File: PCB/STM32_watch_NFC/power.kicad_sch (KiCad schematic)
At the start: 6 parts, among them J2 USB_C_Receptacle_PowerOnly_6P, U2 MIC5365-3.3YC5

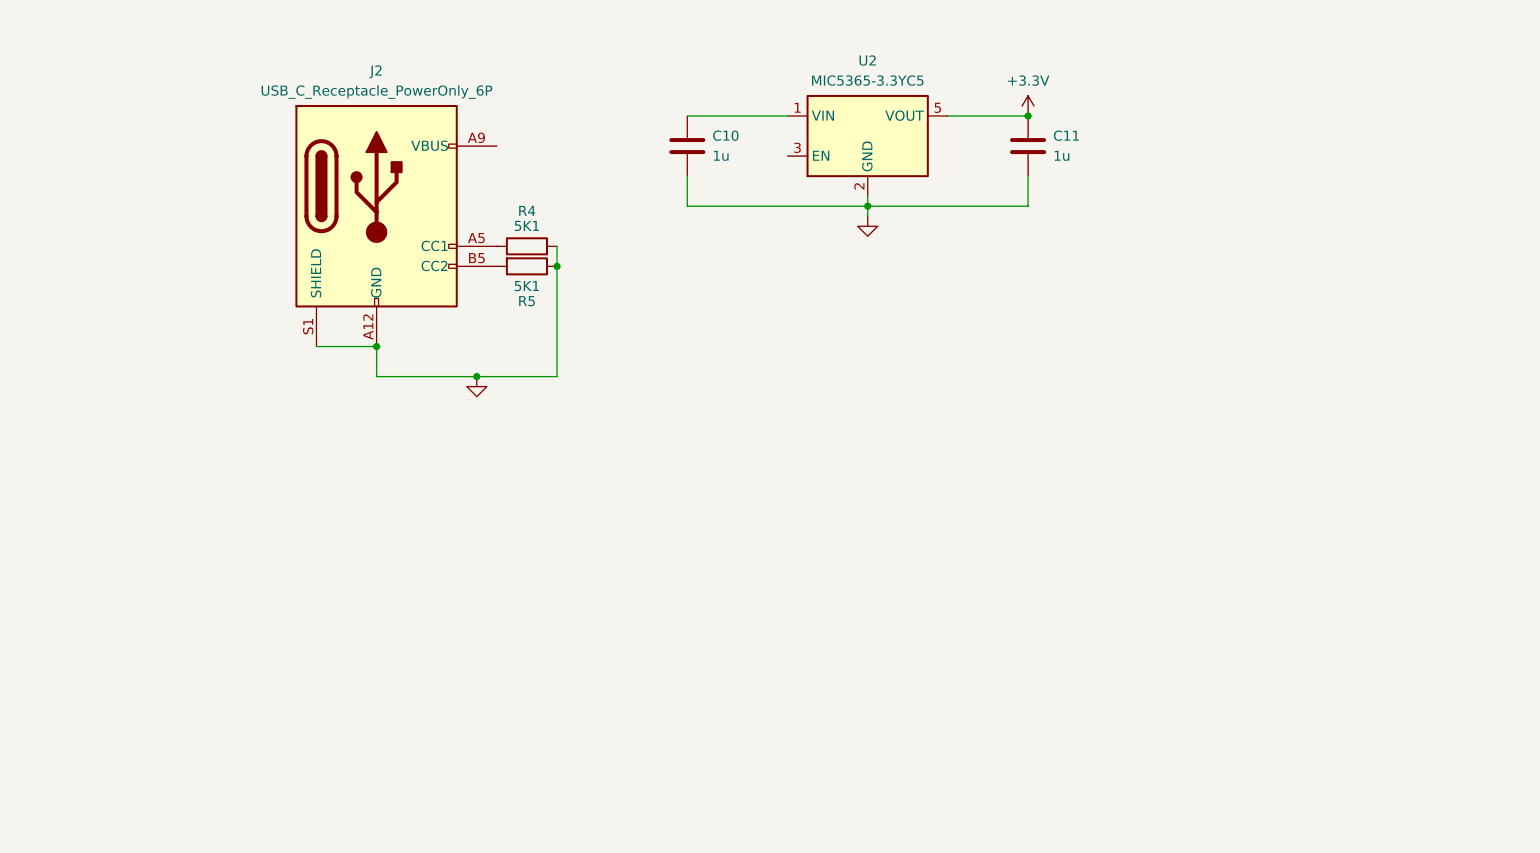
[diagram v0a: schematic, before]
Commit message: Kicad
Everything about power, started to make nfc - spiral antenna problem
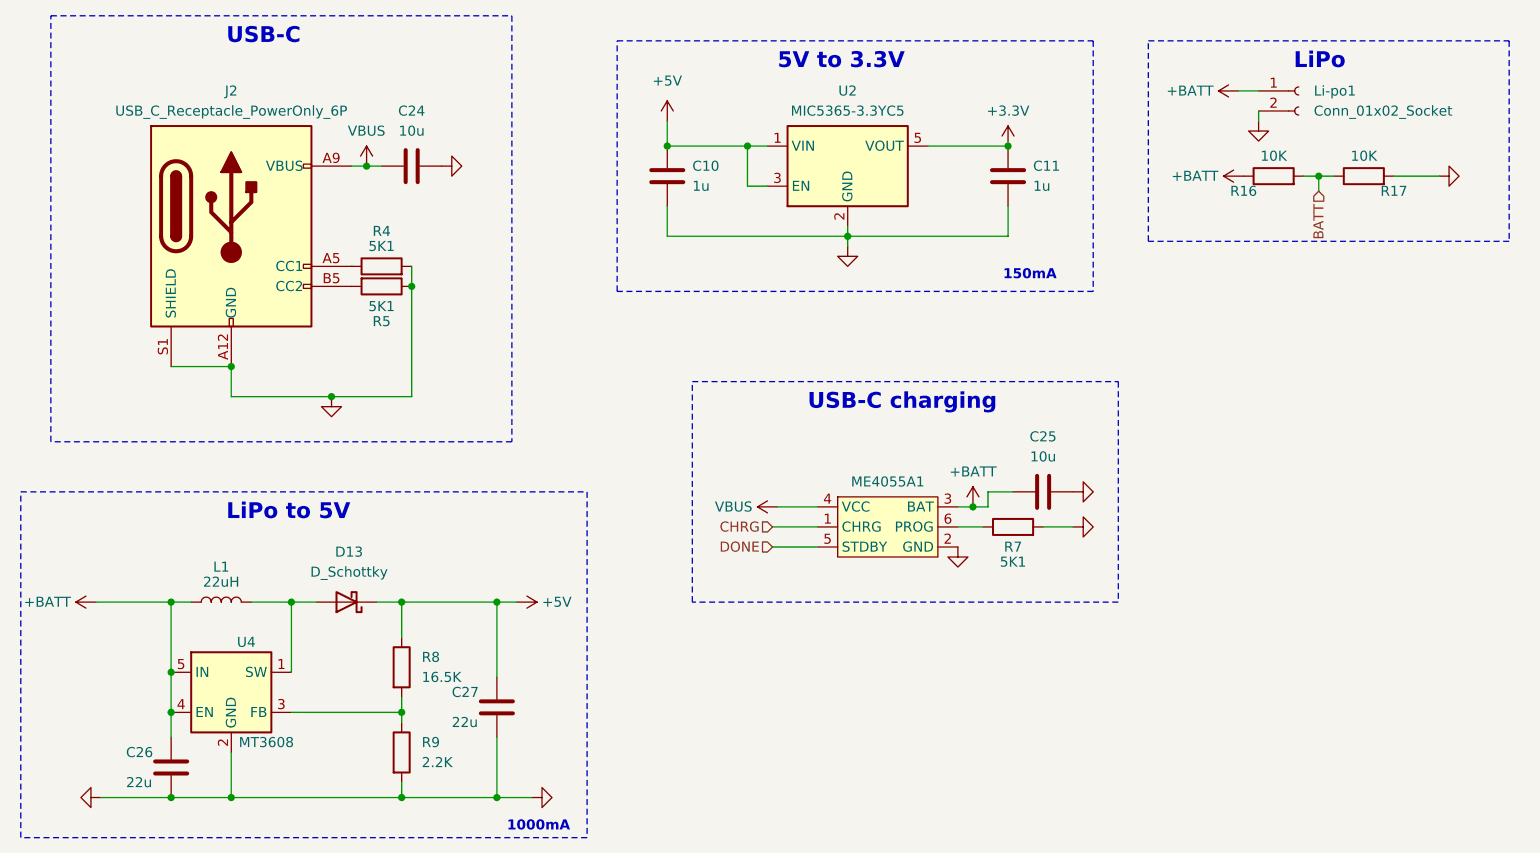
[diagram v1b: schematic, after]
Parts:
- added C24, C25: 10u, Capacitor_SMD:C_0603_1608Metric, symbol Device:C
- added C26, C27: 22u, Capacitor_SMD:C_0603_1608Metric, symbol Device:C
- added D13: D_Schottky, symbol Device:D_Schottky
- added L1: 22uH, symbol Device:L
- added Li-po1: Conn_01x02_Socket, Connector_JST:JST_SUR_SM02B-SURS-TF_1x02-1MP_P0.80mm_Horizontal, symbol Connector:Conn_01x02_Socket
- added ME4055A1: ~, Package_TO_SOT_SMD:SOT-23-6, symbol Power:ME4055AM6G
- added R16, R17: 10K, Resistor_SMD:R_0402_1005Metric, symbol Device:R
- added R7: 5K1, Resistor_SMD:R_0402_1005Metric, symbol Device:R
- added R8: 16.5K, symbol Device:R
- added R9: 2.2K, symbol Device:R
- added U4: MT3608, Package_TO_SOT_SMD:SOT-23-6, symbol Regulator_Switching:MT3608
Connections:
- net GND: now also C24.2, C25.2, C26.2, C27.2, Li-po1.2 (Pin_2), ME4055A1.2 (GND), R17.2, R7.2, R9.2, U4.2 (GND)
- net +5V: now reaches C10.2, U2.1 (VIN)
- net +5V: now also U2.3 (EN), C27.1, D13.1 (K), R8.1
- net VBUS: now reaches J2.A9 (VBUS), J2.B9 (VBUS)
- net VBUS: now also C24.1, ME4055A1.4 (VCC)
- new net: ME4055A1.6 (PROG), R7.1
- new net: R8.2, R9.1, U4.3 (FB)
- new net: D13.2 (A), L1.2, U4.1 (SW)
- new net +BATT: C25.1, C26.1, L1.1, Li-po1.1 (Pin_1), ME4055A1.3 (BAT), R16.1, U4.4 (EN), U4.5 (IN)
- new net BATT: R16.2, R17.1
- new net CHRG: ME4055A1.1 (CHRG)
- new net DONE: ME4055A1.5 (STDBY)
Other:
- note added: "1000mA"
- note added: "150mA"
- note added: "5V to 3.3V"
- note added: "LiPo"
- note added: "LiPo to 5V"
- note added: "USB-C"
- note added: "USB-C charging"
- moved on the sheet: C10, C11, J2, R4, R5, U2

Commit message: Kicad - LCSC, footprints
I managed to add all (I hope so :) ) LCSC values - which component will be used. With that I could determine all footprints
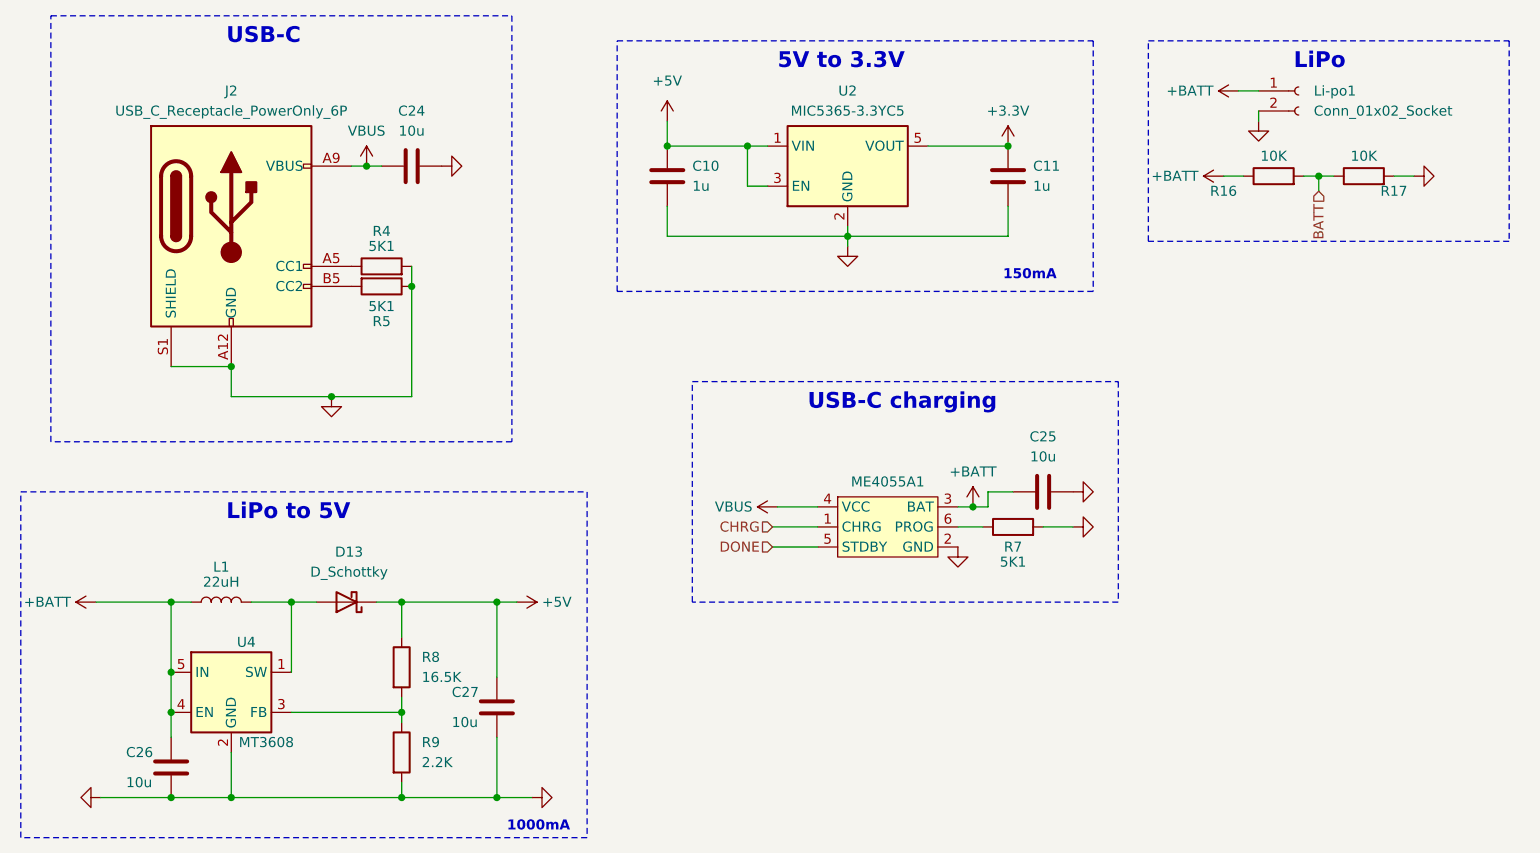
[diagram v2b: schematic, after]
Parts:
- C10, C11: LCSC (none) -> C412453
- C24, C25: LCSC (none) -> C77040
- C26, C27: value 22u -> 10u; LCSC (none) -> C77040
- D13: footprint (none) -> Diode_SMD:D_SOD-523; LCSC (none) -> C145179
- J2: footprint Connector_USB:USB_C_Receptacle_GCT_USB4125-xx-x-0190_6P_TopMnt_Horizontal -> Connector_USB:USB_C_Receptacle_GCT_USB4135-GF-A_6P_TopMnt_Horizontal; LCSC (none) -> C2927283
- L1: footprint (none) -> Components:SLW3015; LCSC (none) -> C206322
- ME4055A1: LCSC (none) -> C610261
- R16, R17: LCSC (none) -> C308028
- R4, R5, R7: LCSC (none) -> C284599
- R8: footprint (none) -> Resistor_SMD:R_0805_2012Metric; LCSC (none) -> C104028
- R9: footprint (none) -> Resistor_SMD:R_0402_1005Metric; LCSC (none) -> C509322
- U2: LCSC (none) -> C3021118
- U4: LCSC (none) -> C84817
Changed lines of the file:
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@@
+    (stroke (width 0) (type default))
+  )
+  (wire (pts (xy 175.895 41.275) (xy 178.435 41.275))
     (stroke (width 0) (type default))
   )
@@
     (stroke (width 0) (type default))
   )
-  (wire (pts (xy 197.485 41.275) (xy 203.2 41.275))
+  (wire (pts (xy 197.485 41.275) (xy 200.025 41.275))
     (stroke (width 0) (type default))
   )
@@
       (effects (font (size 1.27 1.27)) hide)
     )
+    (property "LCSC" "C284599" (at 149.225 85.725 90)
+      (effects (font (size 1.27 1.27)) hide)
+    )
     (pin "1")
     (pin "2")
@@
       (effects (font (size 1.27 1.27)) (justify left))
     )
-    (property "Footprint" "" (at 69.977 114.3 90)
+    (property "Footprint" "Resistor_SMD:R_0402_1005Metric" (at 69.977 114.3 90)
       (effects (font (size 1.27 1.27)) hide)
     )
     (property "Datasheet" "~" (at 71.755 114.3 0)
+      (effects (font (size 1.27 1.27)) hide)
+    )
+    (property "LCSC" "C509322" (at 71.755 114.3 0)
       (effects (font (size 1.27 1.27)) hide)
     )
@@
     )
     (property "Datasheet" "~" (at 105.41 41.275 0)
+      (effects (font (size 1.27 1.27)) hide)
+    )
+    (property "LCSC" "C412453" (at 105.41 41.275 0)
       (effects (font (size 1.27 1.27)) hide)
     )
@@
       (effects (font (size 1.27 1.27)) (justify left))
     )
-    (property "Value" "22u" (at 36.83 118.11 0)
+    (property "Value" "10u" (at 36.83 118.11 0)
       (effects (font (size 1.27 1.27)) (justify left))
     )
@@
     )
     (property "Datasheet" "~" (at 42.545 116.205 0)
+      (effects (font (size 1.27 1.27)) hide)
+    )
+    (property "LCSC" "C77040" (at 42.545 116.205 0)
       (effects (font (size 1.27 1.27)) hide)
     )
@@
       (effects (font (size 1.27 1.27)) (justify left))
     )
-    (property "Value" "22u" (at 78.105 110.49 0)
+    (property "Value" "10u" (at 78.105 110.49 0)
       (effects (font (size 1.27 1.27)) (justify left))
     )
@@
     )
     (property "Datasheet" "~" (at 83.82 108.585 0)
+      (effects (font (size 1.27 1.27)) hide)
+    )
+    (property "LCSC" "C77040" (at 83.82 108.585 0)
       (effects (font (size 1.27 1.27)) hide)
     )
@@
       (effects (font (size 1.27 1.27)))
     )
-    (property "Footprint" "Connector_USB:USB_C_Receptacle_GCT_USB4125-xx-x-0190_6P_TopMnt_Horizontal" (at 53.975 45.085 0)
+    (property "Footprint" "Connector_USB:USB_C_Receptacle_GCT_USB4135-GF-A_6P_TopMnt_Horizontal" (at 53.975 45.085 0)
       (effects (font (size 1.27 1.27)) hide)
     )
     (property "Datasheet" "https://www.usb.org/sites/default/files/documents/usb_type-c.zip" (at 50.165 47.625 0)
+      (effects (font (size 1.27 1.27)) hide)
+    )
+    (property "LCSC" "C2927283" (at 50.165 47.625 0)
       (effects (font (size 1.27 1.27)) hide)
     )
@@
       (effects (font (size 1.27 1.27)) hide)
     )
+    (property "LCSC" "C284599" (at 69.215 55.245 90)
+      (effects (font (size 1.27 1.27)) hide)
+    )
     (pin "1")
     (pin "2")
@@
     )
   )
-  (symbol (lib_id "power:+BATT") (at 178.435 41.275 90) (unit 1)
-    (in_bom yes) (on_board yes) (dnp no) (fields_autoplaced)
-    (property "Reference" "#PWR075" (at 182.245 41.275 0)
-      (effects (font (size 1.27 1.27)) hide)
-    )
-    (property "Value" "+BATT" (at 175.26 41.275 90)
-      (effects (font (size 1.27 1.27)) (justify left))
-    )
-    (property "Footprint" "" (at 178.435 41.275 0)
-      (effects (font (size 1.27 1.27)) hide)
-    )
-    (property "Datasheet" "" (at 178.435 41.275 0)
+  (symbol (lib_id "power:+BATT") (at 175.895 41.275 90) (unit 1)
+    (in_bom yes) (on_board yes) (dnp no) (fields_autoplaced)
+    (property "Reference" "#PWR075" (at 179.705 41.275 0)
+      (effects (font (size 1.27 1.27)) hide)
+    )
+    (property "Value" "+BATT" (at 172.72 41.275 90)
+      (effects (font (size 1.27 1.27)) (justify left))
+    )
+    (property "Footprint" "" (at 175.895 41.275 0)
+      (effects (font (size 1.27 1.27)) hide)
+    )
+    (property "Datasheet" "" (at 175.895 41.275 0)
       (effects (font (size 1.27 1.27)) hide)
     )
@@
       (effects (font (size 1.27 1.27)))
     )
-    (property "Footprint" "" (at 48.895 95.25 0)
+    (property "Footprint" "Components:SLW3015" (at 48.895 95.25 0)
       (effects (font (size 1.27 1.27)) hide)
     )
@@
       (effects (font (size 1.27 1.27)) hide)
     )
+    (property "LCSC" "C206322" (at 48.895 95.25 90)
+      (effects (font (size 1.27 1.27)) hide)
+    )
     (pin "2")
     (pin "1")
@@
     )
   )
-  (symbol (lib_id "power:GND") (at 203.2 41.275 90) (unit 1)
-    (in_bom yes) (on_board yes) (dnp no) (fields_autoplaced)
-    (property "Reference" "#PWR074" (at 209.55 41.275 0)
-      (effects (font (size 1.27 1.27)) hide)
-    )
-    (property "Value" "GND" (at 208.28 41.275 0)
-      (effects (font (size 1.27 1.27)) hide)
-    )
-    (property "Footprint" "" (at 203.2 41.275 0)
-      (effects (font (size 1.27 1.27)) hide)
-    )
-    (property "Datasheet" "" (at 203.2 41.275 0)
+  (symbol (lib_id "power:GND") (at 200.025 41.275 90) (unit 1)
+    (in_bom yes) (on_board yes) (dnp no) (fields_autoplaced)
+    (property "Reference" "#PWR074" (at 206.375 41.275 0)
+      (effects (font (size 1.27 1.27)) hide)
+    )
+    (property "Value" "GND" (at 205.105 41.275 0)
+      (effects (font (size 1.27 1.27)) hide)
+    )
+    (property "Footprint" "" (at 200.025 41.275 0)
+      (effects (font (size 1.27 1.27)) hide)
+    )
+    (property "Datasheet" "" (at 200.025 41.275 0)
       (effects (font (size 1.27 1.27)) hide)
     )
@@
       (effects (font (size 1.27 1.27)) hide)
     )
+    (property "LCSC" "C77040" (at 153.035 81.28 90)
+      (effects (font (size 1.27 1.27)) hide)
+    )
     (pin "2")
     (pin "1")
@@
     )
     (property "Datasheet" "" (at 130.81 84.455 0)
+      (effects (font (size 1.27 1.27)) hide)
+    )
+    (property "LCSC" "C610261" (at 133.35 84.455 0)
       (effects (font (size 1.27 1.27)) hide)
     )
@@
       (effects (font (size 1.27 1.27)))
     )
-    (property "Footprint" "" (at 64.77 95.25 0)
+    (property "Footprint" "Diode_SMD:D_SOD-523" (at 64.77 95.25 0)
       (effects (font (size 1.27 1.27)) hide)
     )
     (property "Datasheet" "~" (at 64.77 95.25 0)
+      (effects (font (size 1.27 1.27)) hide)
+    )
+    (property "LCSC" "C145179" (at 64.77 95.25 0)
       (effects (font (size 1.27 1.27)) hide)
     )
@@
   (symbol (lib_id "Device:R") (at 182.245 41.275 90) (unit 1)
     (in_bom yes) (on_board yes) (dnp no)
-    (property "Reference" "R16" (at 178.435 43.18 90)
+    (property "Reference" "R16" (at 175.895 43.18 90)
       (effects (font (size 1.27 1.27)))
     )
@@
     )
     (property "Datasheet" "~" (at 182.245 41.275 0)
+      (effects (font (size 1.27 1.27)) hide)
+    )
+    (property "LCSC" "C308028" (at 182.245 41.275 90)
       (effects (font (size 1.27 1.27)) hide)
     )
@@
       (effects (font (size 1.27 1.27)) hide)
     )
+    (property "LCSC" "C308028" (at 193.675 41.275 90)
+      (effects (font (size 1.27 1.27)) hide)
+    )
     (pin "1")
     (pin "2")
@@
       (effects (font (size 1.27 1.27)) (justify left))
     )
-    (property "Footprint" "" (at 69.977 103.505 90)
+    (property "Footprint" "Resistor_SMD:R_0805_2012Metric" (at 69.977 103.505 90)
       (effects (font (size 1.27 1.27)) hide)
     )
@@
       (effects (font (size 1.27 1.27)) hide)
     )
+    (property "LCSC" "C104028" (at 71.755 103.505 0)
+      (effects (font (size 1.27 1.27)) hide)
+    )
     (pin "2")
     (pin "1")
@@
     )
     (property "Datasheet" "http://ww1.microchip.com/downloads/en/DeviceDoc/mic5365.pdf" (at 120.65 19.685 0)
+      (effects (font (size 1.27 1.27)) hide)
+    )
+    (property "LCSC" "C3021118" (at 128.27 40.005 0)
       (effects (font (size 1.27 1.27)) hide)
     )
@@
     )
     (property "Datasheet" "~" (at 148.59 41.275 0)
+      (effects (font (size 1.27 1.27)) hide)
+    )
+    (property "LCSC" "C412453" (at 148.59 41.275 0)
       (effects (font (size 1.27 1.27)) hide)
     )
@@
       (effects (font (size 1.27 1.27)) hide)
     )
+    (property "LCSC" "C284599" (at 69.215 52.705 90)
+      (effects (font (size 1.27 1.27)) hide)
+    )
     (pin "1")
     (pin "2")
@@
     )
     (property "Datasheet" "~" (at 73.025 40.005 0)
+      (effects (font (size 1.27 1.27)) hide)
+    )
+    (property "LCSC" "C77040" (at 73.025 40.005 90)
       (effects (font (size 1.27 1.27)) hide)
     )
@@
       (effects (font (size 1.27 1.27)) hide)
     )
+    (property "LCSC" "C84817" (at 50.165 106.68 0)
+      (effects (font (size 1.27 1.27)) hide)
+    )
